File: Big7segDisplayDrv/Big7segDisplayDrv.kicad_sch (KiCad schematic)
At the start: 27 parts, among them J1 Screw_Terminal_01x02, J10 Barrel_Jack_Switch, J2 Screw_Terminal_01x02, J3 Screw_Terminal_01x03, J4 DB9_Male_MountingHoles, J5 DB9_Male_MountingHoles, J6 DB9_Male_MountingHoles, J7 DB9_Male_MountingHoles

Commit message: First version for PCB production.
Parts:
- R1, R2, R3, R4, R5, R6: value (none) -> 1k; footprint (none) -> Resistor_THT:R_Axial_DIN0207_L6.3mm_D2.5mm_P10.16mm_Horizontal
- R10, R11, R12, R7, R8, R9: value (none) -> 4.7k; footprint (none) -> Resistor_THT:R_Axial_DIN0207_L6.3mm_D2.5mm_P10.16mm_Horizontal
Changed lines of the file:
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@@
       (effects (font (size 1.27 1.27)) (justify right))
     )
-    (property "Value" "" (id 1) (at 205.74 38.0999 0)
-      (effects (font (size 1.27 1.27)) (justify right))
-    )
-    (property "Footprint" "" (id 2) (at 204.978 36.83 90)
+    (property "Value" "1k" (id 1) (at 205.74 38.0999 0)
+      (effects (font (size 1.27 1.27)) (justify right))
+    )
+    (property "Footprint" "Resistor_THT:R_Axial_DIN0207_L6.3mm_D2.5mm_P10.16mm_Horizontal" (id 2) (at 204.978 36.83 90)
       (effects (font (size 1.27 1.27)) hide)
     )
@@
     (in_bom yes) (on_board yes) (fields_autoplaced)
     (property "Reference" "R9" (id 0) (at 115.57 53.34 90))
-    (property "Value" "" (id 1) (at 115.57 55.88 90))
-    (property "Footprint" "" (id 2) (at 115.57 57.912 90)
+    (property "Value" "4.7k" (id 1) (at 115.57 55.88 90))
+    (property "Footprint" "Resistor_THT:R_Axial_DIN0207_L6.3mm_D2.5mm_P10.16mm_Horizontal" (id 2) (at 115.57 57.912 90)
       (effects (font (size 1.27 1.27)) hide)
     )
@@
       (effects (font (size 1.27 1.27)) (justify right))
     )
-    (property "Value" "" (id 1) (at 190.5 38.0999 0)
-      (effects (font (size 1.27 1.27)) (justify right))
-    )
-    (property "Footprint" "" (id 2) (at 189.738 36.83 90)
+    (property "Value" "1k" (id 1) (at 190.5 38.0999 0)
+      (effects (font (size 1.27 1.27)) (justify right))
+    )
+    (property "Footprint" "Resistor_THT:R_Axial_DIN0207_L6.3mm_D2.5mm_P10.16mm_Horizontal" (id 2) (at 189.738 36.83 90)
       (effects (font (size 1.27 1.27)) hide)
     )
@@
     (in_bom yes) (on_board yes) (fields_autoplaced)
     (property "Reference" "R10" (id 0) (at 123.19 55.88 90))
-    (property "Value" "" (id 1) (at 123.19 58.42 90))
-    (property "Footprint" "" (id 2) (at 123.19 60.452 90)
+    (property "Value" "4.7k" (id 1) (at 123.19 58.42 90))
+    (property "Footprint" "Resistor_THT:R_Axial_DIN0207_L6.3mm_D2.5mm_P10.16mm_Horizontal" (id 2) (at 123.19 60.452 90)
       (effects (font (size 1.27 1.27)) hide)
     )
@@
     (in_bom yes) (on_board yes) (fields_autoplaced)
     (property "Reference" "R7" (id 0) (at 121.92 40.64 90))
-    (property "Value" "" (id 1) (at 121.92 43.18 90))
-    (property "Footprint" "" (id 2) (at 121.92 45.212 90)
+    (property "Value" "4.7k" (id 1) (at 121.92 43.18 90))
+    (property "Footprint" "Resistor_THT:R_Axial_DIN0207_L6.3mm_D2.5mm_P10.16mm_Horizontal" (id 2) (at 121.92 45.212 90)
       (effects (font (size 1.27 1.27)) hide)
     )
@@
       (effects (font (size 1.27 1.27)) (justify right))
     )
-    (property "Value" "" (id 1) (at 182.88 38.0999 0)
-      (effects (font (size 1.27 1.27)) (justify right))
-    )
-    (property "Footprint" "" (id 2) (at 182.118 36.83 90)
+    (property "Value" "1k" (id 1) (at 182.88 38.0999 0)
+      (effects (font (size 1.27 1.27)) (justify right))
+    )
+    (property "Footprint" "Resistor_THT:R_Axial_DIN0207_L6.3mm_D2.5mm_P10.16mm_Horizontal" (id 2) (at 182.118 36.83 90)
       (effects (font (size 1.27 1.27)) hide)
     )
@@
     (in_bom yes) (on_board yes) (fields_autoplaced)
     (property "Reference" "R12" (id 0) (at 110.49 68.58 90))
-    (property "Value" "" (id 1) (at 110.49 71.12 90))
-    (property "Footprint" "" (id 2) (at 110.49 73.152 90)
+    (property "Value" "4.7k" (id 1) (at 110.49 71.12 90))
+    (property "Footprint" "Resistor_THT:R_Axial_DIN0207_L6.3mm_D2.5mm_P10.16mm_Horizontal" (id 2) (at 110.49 73.152 90)
       (effects (font (size 1.27 1.27)) hide)
     )
@@
     (in_bom yes) (on_board yes) (fields_autoplaced)
     (property "Reference" "R11" (id 0) (at 123.19 66.04 90))
-    (property "Value" "" (id 1) (at 123.19 68.58 90))
-    (property "Footprint" "" (id 2) (at 123.19 70.612 90)
+    (property "Value" "4.7k" (id 1) (at 123.19 68.58 90))
+    (property "Footprint" "Resistor_THT:R_Axial_DIN0207_L6.3mm_D2.5mm_P10.16mm_Horizontal" (id 2) (at 123.19 70.612 90)
       (effects (font (size 1.27 1.27)) hide)
     )
@@
       (effects (font (size 1.27 1.27)) (justify right))
     )
-    (property "Value" "" (id 1) (at 167.64 38.0999 0)
-      (effects (font (size 1.27 1.27)) (justify right))
-    )
-    (property "Footprint" "" (id 2) (at 166.878 36.83 90)
+    (property "Value" "1k" (id 1) (at 167.64 38.0999 0)
+      (effects (font (size 1.27 1.27)) (justify right))
+    )
+    (property "Footprint" "Resistor_THT:R_Axial_DIN0207_L6.3mm_D2.5mm_P10.16mm_Horizontal" (id 2) (at 166.878 36.83 90)
       (effects (font (size 1.27 1.27)) hide)
     )
@@
       (effects (font (size 1.27 1.27)) (justify right))
     )
-    (property "Value" "" (id 1) (at 198.12 38.0999 0)
-      (effects (font (size 1.27 1.27)) (justify right))
-    )
-    (property "Footprint" "" (id 2) (at 197.358 36.83 90)
+    (property "Value" "1k" (id 1) (at 198.12 38.0999 0)
+      (effects (font (size 1.27 1.27)) (justify right))
+    )
+    (property "Footprint" "Resistor_THT:R_Axial_DIN0207_L6.3mm_D2.5mm_P10.16mm_Horizontal" (id 2) (at 197.358 36.83 90)
       (effects (font (size 1.27 1.27)) hide)
     )
@@
     (in_bom yes) (on_board yes) (fields_autoplaced)
     (property "Reference" "R8" (id 0) (at 113.03 43.18 90))
-    (property "Value" "" (id 1) (at 113.03 45.72 90))
-    (property "Footprint" "" (id 2) (at 113.03 47.752 90)
+    (property "Value" "4.7k" (id 1) (at 113.03 45.72 90))
+    (property "Footprint" "Resistor_THT:R_Axial_DIN0207_L6.3mm_D2.5mm_P10.16mm_Horizontal" (id 2) (at 113.03 47.752 90)
       (effects (font (size 1.27 1.27)) hide)
     )
@@
       (effects (font (size 1.27 1.27)) (justify right))
     )
-    (property "Value" "" (id 1) (at 175.26 38.0999 0)
-      (effects (font (size 1.27 1.27)) (justify right))
-    )
-    (property "Footprint" "" (id 2) (at 174.498 36.83 90)
+    (property "Value" "1k" (id 1) (at 175.26 38.0999 0)
+      (effects (font (size 1.27 1.27)) (justify right))
+    )
+    (property "Footprint" "Resistor_THT:R_Axial_DIN0207_L6.3mm_D2.5mm_P10.16mm_Horizontal" (id 2) (at 174.498 36.83 90)
       (effects (font (size 1.27 1.27)) hide)
     )
@@
     )
     (path "/7d9221cc-bef3-465f-b042-5fec8f114db9"
-      (reference "Q1") (unit 1) (value "BC548") (footprint "Package_TO_SOT_THT:TO-92_Inline")
+      (reference "Q1") (unit 1) (value "BC548") (footprint "Package_TO_SOT_THT:TO-92_HandSolder")
     )
     (path "/4b76b72a-cd52-4c96-bcd7-b7eb37e45a71"
-      (reference "Q2") (unit 1) (value "BC548") (footprint "Package_TO_SOT_THT:TO-92_Inline")
+      (reference "Q2") (unit 1) (value "BC548") (footprint "Package_TO_SOT_THT:TO-92_HandSolder")
     )
     (path "/ec0022a3-b763-4968-bab2-da03f869dff4"
-      (reference "Q3") (unit 1) (value "BC548") (footprint "Package_TO_SOT_THT:TO-92_Inline")
+      (reference "Q3") (unit 1) (value "BC548") (footprint "Package_TO_SOT_THT:TO-92_HandSolder")
     )
     (path "/c3b10306-ffea-4360-a540-14b7f64a3a06"
-      (reference "Q4") (unit 1) (value "BC548") (footprint "Package_TO_SOT_THT:TO-92_Inline")
+      (reference "Q4") (unit 1) (value "BC548") (footprint "Package_TO_SOT_THT:TO-92_HandSolder")
     )
     (path "/1e1a4370-2f3f-446d-afc2-bb99181a4991"
-      (reference "Q5") (unit 1) (value "BC548") (footprint "Package_TO_SOT_THT:TO-92_Inline")
+      (reference "Q5") (unit 1) (value "BC548") (footprint "Package_TO_SOT_THT:TO-92_HandSolder")
     )
     (path "/7b56d902-fe20-4bc8-9b02-21b6ea4acbc9"
-      (reference "Q6") (unit 1) (value "BC548") (footprint "Package_TO_SOT_THT:TO-92_Inline")
+      (reference "Q6") (unit 1) (value "BC548") (footprint "Package_TO_SOT_THT:TO-92_HandSolder")
     )
     (path "/c13eee10-4bba-466f-a9fe-a5907705f6d9"

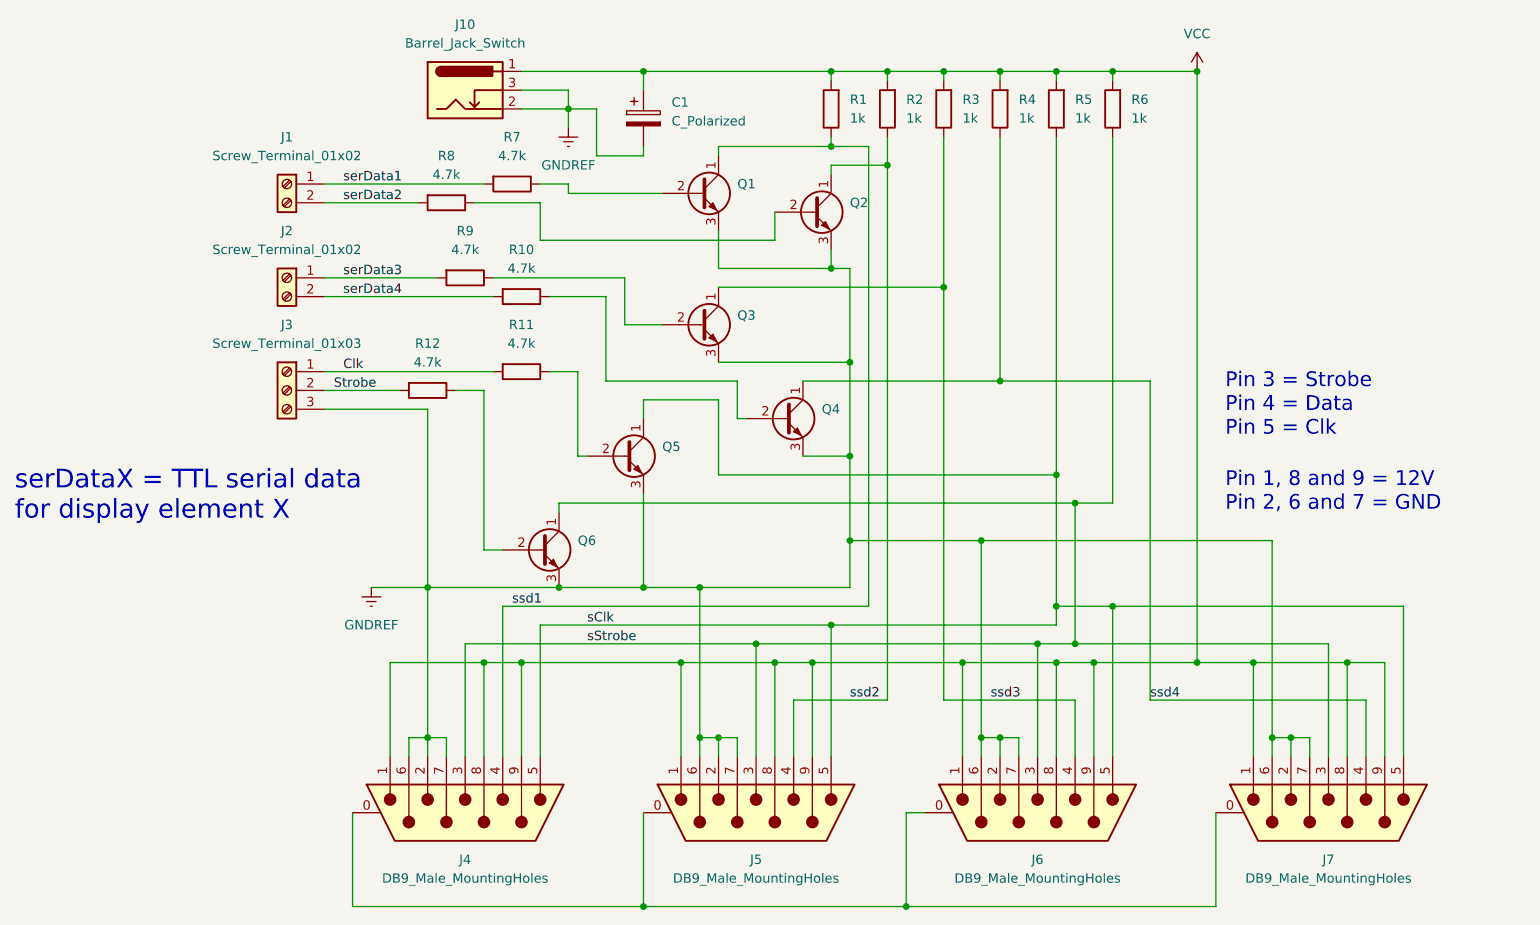
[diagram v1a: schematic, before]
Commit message: Big7segDisplay prototype prod. completed.
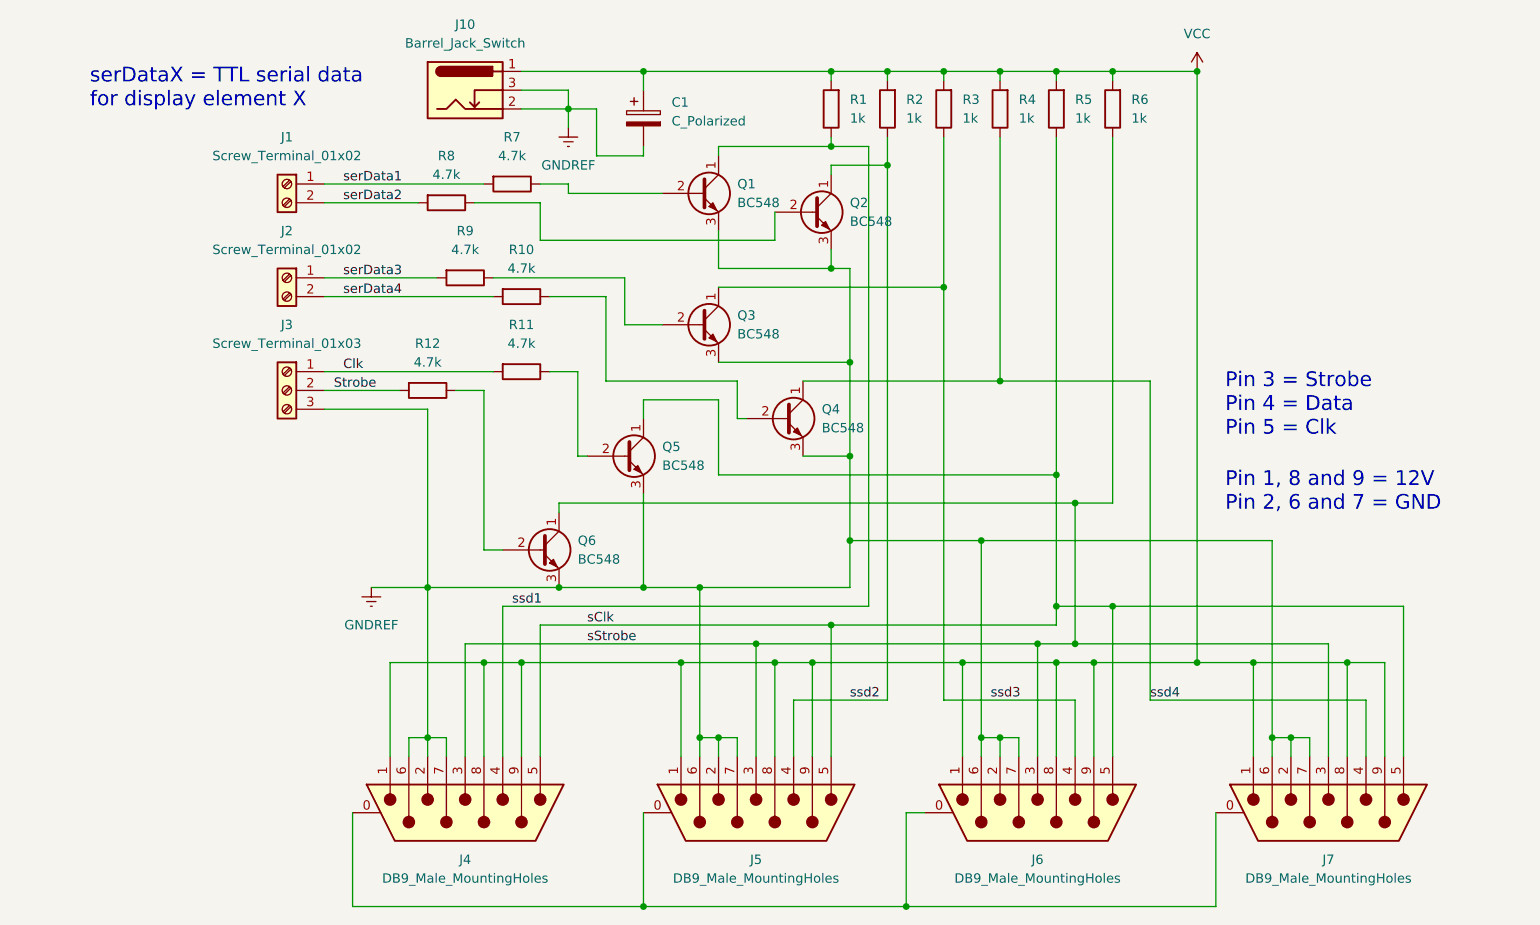
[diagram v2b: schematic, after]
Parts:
- Q1, Q2, Q3, Q4, Q5, Q6: value (none) -> BC548; footprint (none) -> Package_TO_SOT_THT:TO-92_HandSolder
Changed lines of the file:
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@@
     (effects (font (size 2 2)) (justify left bottom))
   )
-  (text "serDataX = TTL serial data \nfor display element X" (at 54.61 92.71 0)
-    (effects (font (size 2.54 2.54)) (justify left bottom))
+  (text "serDataX = TTL serial data \nfor display element X" (at 64.77 36.83 0)
+    (effects (font (size 2 2)) (justify left bottom))
   )
   (label "Strobe" (at 97.79 74.93 0)
@@
       (effects (font (size 1.27 1.27)) (justify left))
     )
-    (property "Value" "" (id 1) (at 142.24 85.0899 0)
-      (effects (font (size 1.27 1.27)) (justify left))
-    )
-    (property "Footprint" "" (id 2) (at 142.24 85.725 0)
+    (property "Value" "BC548" (id 1) (at 142.24 85.0899 0)
+      (effects (font (size 1.27 1.27)) (justify left))
+    )
+    (property "Footprint" "Package_TO_SOT_THT:TO-92_HandSolder" (id 2) (at 142.24 85.725 0)
       (effects (font (size 1.27 1.27) italic) (justify left) hide)
     )
@@
       (effects (font (size 1.27 1.27)) (justify left))
     )
-    (property "Value" "" (id 1) (at 167.64 52.0699 0)
-      (effects (font (size 1.27 1.27)) (justify left))
-    )
-    (property "Footprint" "" (id 2) (at 167.64 52.705 0)
+    (property "Value" "BC548" (id 1) (at 167.64 52.0699 0)
+      (effects (font (size 1.27 1.27)) (justify left))
+    )
+    (property "Footprint" "Package_TO_SOT_THT:TO-92_HandSolder" (id 2) (at 167.64 52.705 0)
       (effects (font (size 1.27 1.27) italic) (justify left) hide)
     )
@@
       (effects (font (size 1.27 1.27)) (justify left))
     )
-    (property "Value" "" (id 1) (at 130.81 97.7899 0)
-      (effects (font (size 1.27 1.27)) (justify left))
-    )
-    (property "Footprint" "" (id 2) (at 130.81 98.425 0)
+    (property "Value" "BC548" (id 1) (at 130.81 97.7899 0)
+      (effects (font (size 1.27 1.27)) (justify left))
+    )
+    (property "Footprint" "Package_TO_SOT_THT:TO-92_HandSolder" (id 2) (at 130.81 98.425 0)
       (effects (font (size 1.27 1.27) italic) (justify left) hide)
     )
@@
       (effects (font (size 1.27 1.27)) (justify left))
     )
-    (property "Value" "" (id 1) (at 152.4 49.5299 0)
-      (effects (font (size 1.27 1.27)) (justify left))
-    )
-    (property "Footprint" "" (id 2) (at 152.4 50.165 0)
+    (property "Value" "BC548" (id 1) (at 152.4 49.5299 0)
+      (effects (font (size 1.27 1.27)) (justify left))
+    )
+    (property "Footprint" "Package_TO_SOT_THT:TO-92_HandSolder" (id 2) (at 152.4 50.165 0)
       (effects (font (size 1.27 1.27) italic) (justify left) hide)
     )
@@
       (effects (font (size 1.27 1.27)) (justify left))
     )
-    (property "Value" "" (id 1) (at 163.83 80.0099 0)
-      (effects (font (size 1.27 1.27)) (justify left))
-    )
-    (property "Footprint" "" (id 2) (at 163.83 80.645 0)
+    (property "Value" "BC548" (id 1) (at 163.83 80.0099 0)
+      (effects (font (size 1.27 1.27)) (justify left))
+    )
+    (property "Footprint" "Package_TO_SOT_THT:TO-92_HandSolder" (id 2) (at 163.83 80.645 0)
       (effects (font (size 1.27 1.27) italic) (justify left) hide)
     )
@@
       (effects (font (size 1.27 1.27)) (justify left))
     )
-    (property "Value" "" (id 1) (at 152.4 67.3099 0)
-      (effects (font (size 1.27 1.27)) (justify left))
-    )
-    (property "Footprint" "" (id 2) (at 152.4 67.945 0)
-      (effects (font (size 1.27 1.27) italic) (justify left) hide)
-    )
+    (property "Value" "BC548" (id 1) (at 152.4 67.3099 0)
+      (effects (font (size 1.27 1.27)) (justify left))
+    )
+    (property "Footprint" "Package_TO_SOT_THT:TO-92_HandSolder" (id 2) (at 152.4 67.945 0)
+      (effects (font (size 1.27 1.27) italic) (justify left) hide)
+    )
